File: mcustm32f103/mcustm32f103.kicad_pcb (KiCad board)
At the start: 2 copper layers, 76.2 x 50.8 mm, 31 parts, among them J2 STM32WORLD_BASE, U1 AMS1117-3.3, U2 STM32F405RGTx, U3 SRV05-4, Y1 X_16MHZ

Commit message: Hmmm
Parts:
- removed C12, C9: C_2.2UF_0603, Capacitor_SMD:C_0603_1608Metric
- removed U3: SRV05-4, Package_TO_SOT_SMD:SOT-23-6
- U2: value STM32F405RGTx -> STM32F103CBTx; footprint Package_QFP:LQFP-64_10x10mm_P0.5mm -> Package_QFP:LQFP-48_7x7mm_P0.5mm
- moved C8 8.98 mm to (157.5, 108.6), turned to 0 degrees
- moved R3 3.81 mm to (178.4, 104.8)
- moved R4 3.81 mm to (178.4, 99.1)
- moved R5 3.81 mm to (178.4, 102.9)
- moved R6 3.81 mm to (178.4, 101.0)
- moved C6 3.65 mm to (157.5, 96.5)
- moved C4 2.62 mm to (157.5, 106.7)
- moved C5 2.29 mm to (147.3, 96.5)
- moved C7 1.27 mm to (141.0, 105.4)
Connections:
- U2 pad 10: PC2 -> PA0
- U2 pad 11: PC3 -> PA1
- U2 pad 12: GND -> PA2
- U2 pad 13: +3V3 -> PA3
- U2 pad 14: PA0 -> PA4
- U2 pad 15: PA1 -> PA5
- U2 pad 16: PA2 -> PA6
- U2 pad 17: PA3 -> PA7
- U2 pad 18: GND -> PB0
- U2 pad 19: +3V3 -> PB1
- U2 pad 20: PA4 -> PB2
- U2 pad 21: PA5 -> PB10
- U2 pad 22: PA6 -> PB11
- U2 pad 23: PA7 -> GND
- U2 pad 24: PC4 -> +3V3
- U2 pad 25: PC5 -> PB12
- U2 pad 26: PB0 -> PB13
- U2 pad 27: PB1 -> PB14
- U2 pad 28: PB2 -> PB15
- U2 pad 29: PB10 -> PA8
- U2 pad 30: PB11 -> PA9
- U2 pad 31: Net-(C9-Pad1) -> PA10
- U2 pad 32: +3V3 -> PA11
- U2 pad 33: PB12 -> PA12
- U2 pad 34: PB13 -> PA13
- U2 pad 35: PB14 -> GND
- U2 pad 36: PB15 -> +3V3
- U2 pad 37: PC6 -> PA14
- U2 pad 38: PC7 -> PA15
- U2 pad 39: PC8 -> PB3
- U2 pad 40: PC9 -> PB4
- U2 pad 41: PA8 -> PB5
- U2 pad 42: PA9 -> PB6
- U2 pad 43: PA10 -> PB7
- U2 pad 44: PA11 -> BO0
- U2 pad 45: PA12 -> PB8
- U2 pad 46: PA13 -> PB9
- U2 pad 47: Net-(C12-Pad1) -> GND
- U2 pad 8: PC0 -> GND
- U2 pad 9: PC1 -> +3V3
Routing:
- net PC0: track 30.1 -> 0.00 mm
- net PC2: track 28.0 -> 0.00 mm
- net PC1: track 26.1 -> 0.00 mm
- net PC8: track 24.2 -> 0.00 mm
- net PC3: track 24.1 -> 0.00 mm
- net +3V3: track 280.8 -> 257.9 mm, vias 14 -> 13
- net PC6: track 22.3 -> 0.00 mm
- net PC9: track 22.3 -> 0.00 mm
- net PC7: track 19.9 -> 0.00 mm
- net PD2: track 17.1 -> 0.00 mm
- net PC4: track 17.0 -> 0.00 mm
- net PC12: track 15.9 -> 0.00 mm
- net PC10: track 15.3 -> 0.00 mm
- net PC5: track 13.8 -> 0.00 mm
- net PC11: track 12.5 -> 0.00 mm
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
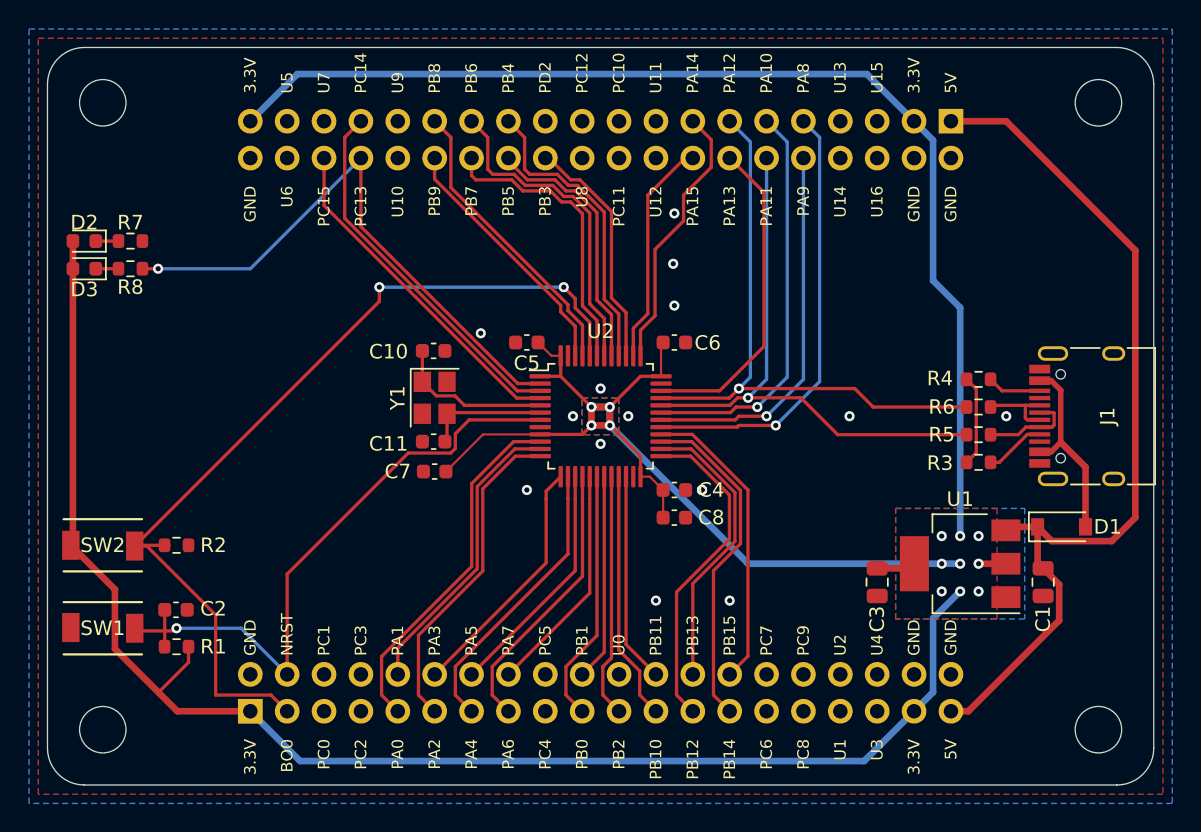
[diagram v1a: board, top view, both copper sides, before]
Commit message: Added SPI Flash Module MEMW25Q128
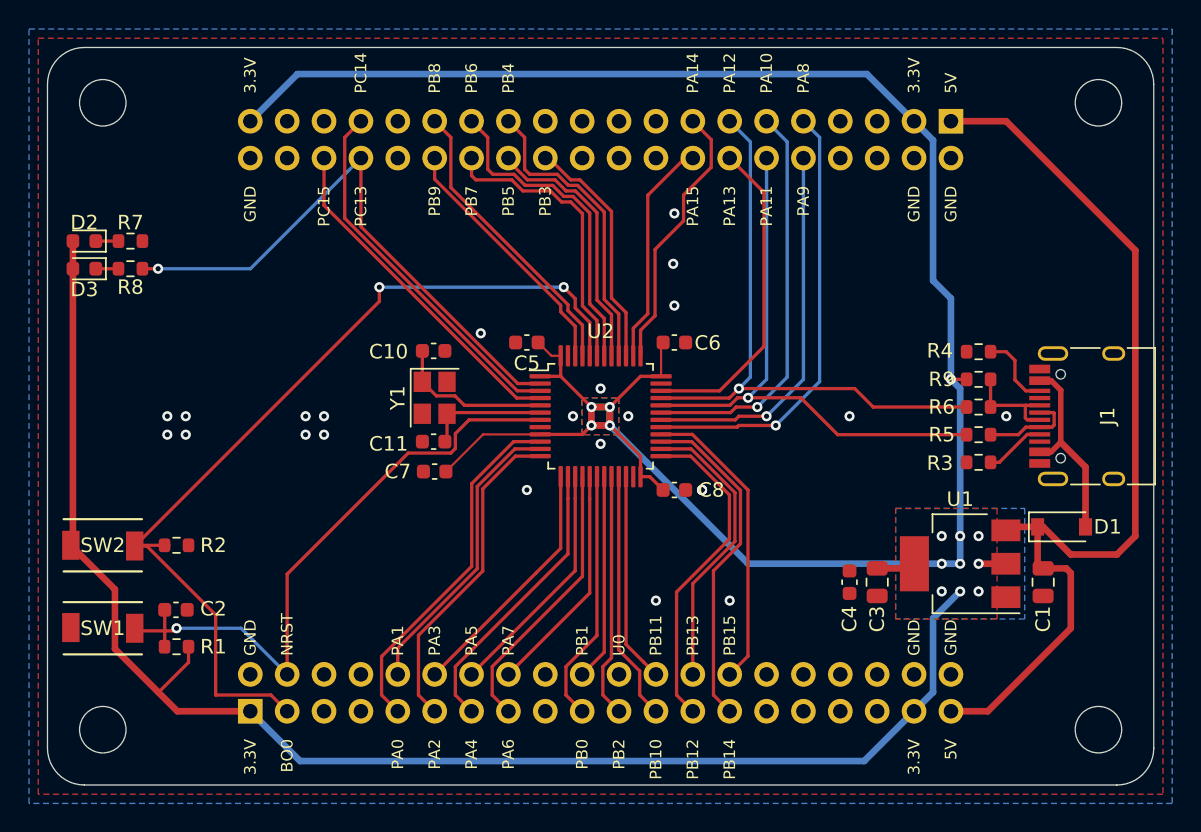
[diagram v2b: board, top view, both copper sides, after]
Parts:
- added R9: R_1.5K_0603, Resistor_SMD:R_0603_1608Metric, F.Cu at (178.4, 99.1)
- moved C4 13.6 mm to (169.5, 113.0), turned to 270 degrees
- moved R4 1.91 mm to (178.4, 97.2)
- moved C8 1.90 mm to (157.5, 106.7)
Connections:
- R3 pad 1: UCC -> GND
- R4 pad 1: UCC -> GND
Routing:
- net UCC: track 6.27 -> 0.00 mm
- net +5V: track 62.0 -> 65.9 mm
- net Net-(J1-PadA6): track 5.36 -> 7.27 mm
- net Net-(J1-PadB5): track 3.71 -> 5.29 mm
- net +3V3: track 257.9 -> 259.0 mm, vias 13 -> 14
- net GND: vias 15 -> 23

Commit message: Hmmm
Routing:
- net PA3: track 17.2 -> 20.4 mm
- net PA4: track 19.8 -> 22.8 mm
- net PA5: track 16.6 -> 18.9 mm
- net PA13: track 22.3 -> 20.1 mm
- net PA6: track 19.2 -> 21.3 mm
- net PA14: track 18.7 -> 20.6 mm
- net PB12: track 22.7 -> 24.5 mm
- net PA7: track 15.9 -> 17.4 mm
- net PB13: track 20.1 -> 21.2 mm
- net PB14: track 23.3 -> 24.4 mm
- net PB15: track 20.8 -> 21.7 mm
- net PB3: track 16.4 -> 17.4 mm
- net PB5: track 18.0 -> 19.0 mm
- net PB4: track 20.8 -> 21.7 mm
- net PB6: track 22.3 -> 23.2 mm
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
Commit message: Hmmmm
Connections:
- J1 pad A8: Net-(J1-PadA8) -> unconnected-(J1-PadA8)
- J1 pad B8: Net-(J1-PadB8) -> unconnected-(J1-PadB8)
- J2 pad 22: Net-(J2-Pad22) -> unconnected-(J2-Pad22)
- J2 pad 33: Net-(J2-Pad33) -> unconnected-(J2-Pad33)
- J2 pad 34: Net-(J2-Pad34) -> unconnected-(J2-Pad34)
- J2 pad 35: Net-(J2-Pad35) -> unconnected-(J2-Pad35)
- J2 pad 36: Net-(J2-Pad36) -> unconnected-(J2-Pad36)
- J2 pad 45: Net-(J2-Pad45) -> unconnected-(J2-Pad45)
- J2 pad 46: Net-(J2-Pad46) -> unconnected-(J2-Pad46)
- J2 pad 47: Net-(J2-Pad47) -> unconnected-(J2-Pad47)
- J2 pad 48: Net-(J2-Pad48) -> unconnected-(J2-Pad48)
- J2 pad 57: Net-(J2-Pad57) -> unconnected-(J2-Pad57)
- J2 pad 58: Net-(J2-Pad58) -> unconnected-(J2-Pad58)
- J2 pad 62: Net-(J2-Pad62) -> unconnected-(J2-Pad62)
- J2 pad 71: Net-(J2-Pad71) -> unconnected-(J2-Pad71)
- J2 pad 72: Net-(J2-Pad72) -> unconnected-(J2-Pad72)
- J2 pad 75: Net-(J2-Pad75) -> unconnected-(J2-Pad75)
- J2 pad 77: Net-(J2-Pad77) -> unconnected-(J2-Pad77)
- J2 pad 78: Net-(J2-Pad78) -> unconnected-(J2-Pad78)
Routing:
- net VBUS: track 13.6 -> 17.6 mm
- net +3V3: track 259.0 -> 260.9 mm
- net BO0: track 64.0 -> 62.5 mm
- net +5V: track 65.9 -> 65.1 mm
- net GND: vias 23 -> 25
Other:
- net class Default removed
